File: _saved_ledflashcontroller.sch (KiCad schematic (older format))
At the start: 23 parts, among them J1 Conn_02x08_Odd_Even, J2 CONN_01X02, J3 CONN_01X02, K1 LDD-1000H, K2 LDD-1000H, P1 V_IN, P2 I2C_HEADER, P3 GPIO_HEADER, P4 V_DIM1, P5 V_DIM2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

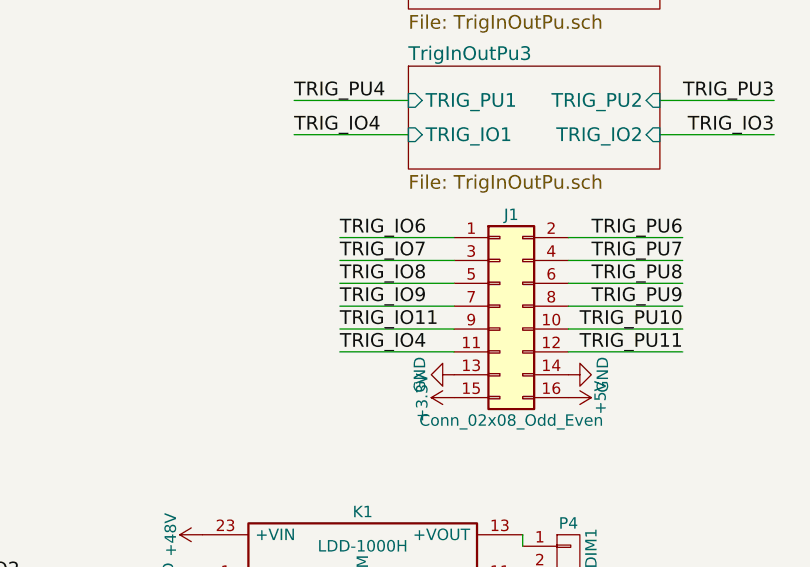
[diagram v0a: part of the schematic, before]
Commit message: Bugfixes for vias to close to wires
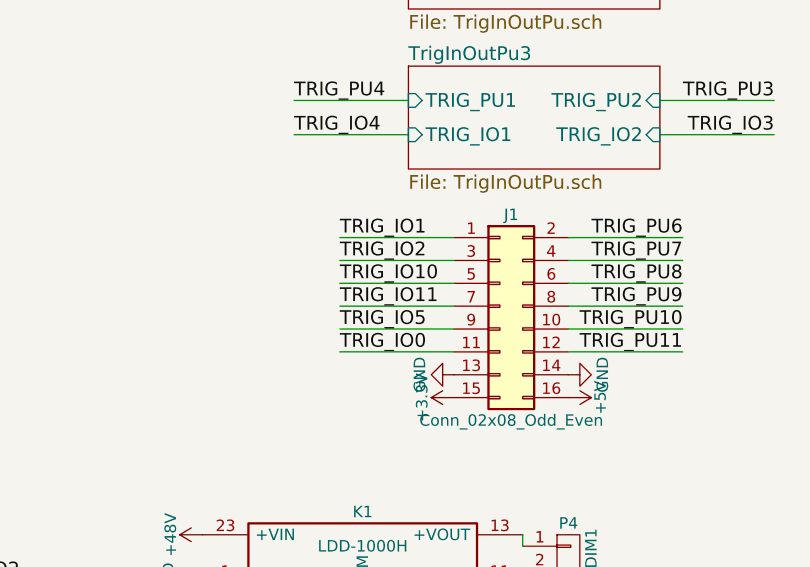
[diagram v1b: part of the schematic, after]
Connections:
- net TRIG_IO0: now also J1.11 (Pin_11)
- net TRIG_IO1: now also J1.1 (Pin_1)
- net TRIG_IO10: now also J1.5 (Pin_5)
- net TRIG_IO11: now also J1.7 (Pin_7); no longer J1.9 (Pin_9)
- net TRIG_IO2: now also J1.3 (Pin_3)
- net TRIG_IO4: no longer J1.11 (Pin_11)
- net TRIG_IO5: now also J1.9 (Pin_9)
- net TRIG_IO6: no longer J1.1 (Pin_1)
- net TRIG_IO7: no longer J1.3 (Pin_3)
- net TRIG_IO8: no longer J1.5 (Pin_5)
- net TRIG_IO9: no longer J1.7 (Pin_7)
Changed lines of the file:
@@
 	5650 3550 5150 3550
 Text Label 5150 3550 0    60   ~ 0
-TRIG_IO4
+TRIG_IO0
 Wire Wire Line
 	5650 3450 5150 3450
 Text Label 5150 3450 0    60   ~ 0
-TRIG_IO11
+TRIG_IO5
 Wire Wire Line
 	5650 3350 5150 3350
 Text Label 5150 3350 0    60   ~ 0
-TRIG_IO9
+TRIG_IO11
 Wire Wire Line
 	5650 3250 5150 3250
 Text Label 5150 3250 0    60   ~ 0
-TRIG_IO8
+TRIG_IO10
 Wire Wire Line
 	5650 3150 5150 3150
 Text Label 5150 3150 0    60   ~ 0
-TRIG_IO7
+TRIG_IO2
 Wire Wire Line
 	5650 3050 5150 3050
 Text Label 5150 3050 0    60   ~ 0
-TRIG_IO6
+TRIG_IO1
 Wire Wire Line
 	6150 3050 6650 3050
